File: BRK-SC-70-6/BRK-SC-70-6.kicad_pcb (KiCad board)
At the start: 2 copper layers, 18.3 x 18 mm, 3 parts, among them J1 Conn_01x03, J2 Conn_01x03, U1 SC-70-6

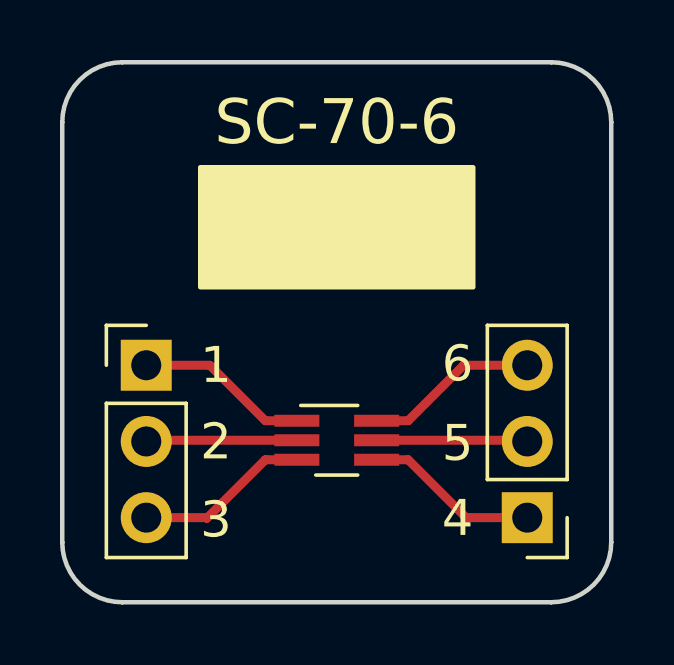
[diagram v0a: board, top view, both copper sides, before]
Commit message: Update several breakout boards
* Reduce distance from edge to pin header
* Enlarge silk screen area
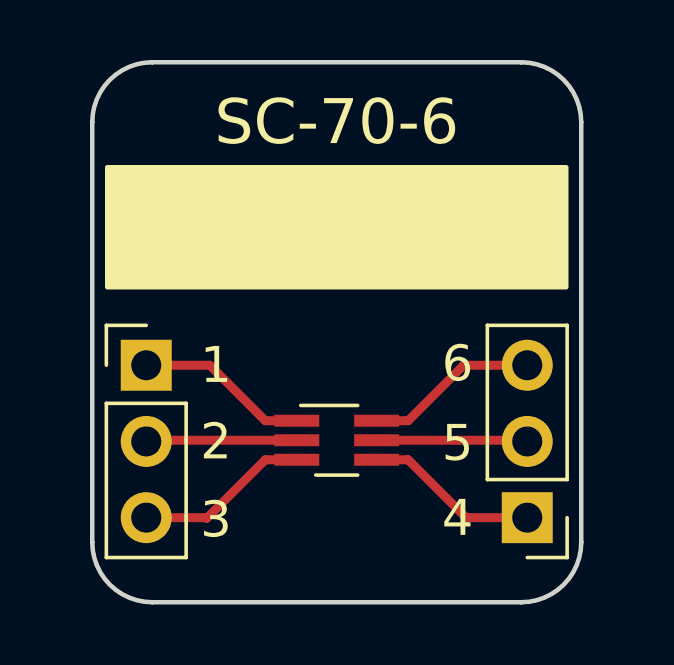
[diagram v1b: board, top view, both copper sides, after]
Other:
- board size 18.3 x 18 mm -> 16.3 x 18 mm
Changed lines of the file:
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@@
-(kicad_pcb (version 20171130) (host pcbnew 5.0.1-33cea8e~68~ubuntu18.10.1)
+(kicad_pcb (version 20171130) (host pcbnew 5.1.4-e60b266~84~ubuntu19.04.1)
   (general
-    (thickness 1.6)
+    (thickness 1)
     (drawings 16)
     (tracks 18)
@@
   (title_block
     (title BRK-SC-70-6)
-    (rev v1.0)
+    (rev v1.1)
     (company https://gekkio.fi)
   )
@@
     (zone_45_only no)
     (trace_min 0.2)
-    (segment_width 0.2)
-    (edge_width 0.15)
     (via_size 0.8)
     (via_drill 0.4)
@@
     (uvia_min_size 0.2)
     (uvia_min_drill 0.1)
+    (edge_width 0.15)
+    (segment_width 0.2)
     (pcb_text_width 0.3)
     (pcb_text_size 1.5 1.5)
@@
     (fp_line (start 1.27 -1.27) (end 1.27 6.35) (layer F.Fab) (width 0.1))
     (fp_line (start -0.635 -1.27) (end 1.27 -1.27) (layer F.Fab) (width 0.1))
-    (pad 3 thru_hole oval (at 0 5.08) (size 1.7 1.7) (drill 1) (layers *.Cu *.Mask)
+    (pad 3 thru_hole oval (at 0 5.08 180) (size 1.7 1.7) (drill 1) (layers *.Cu *.Mask)
       (net 6 "Net-(J2-Pad3)"))
-    (pad 2 thru_hole oval (at 0 2.54) (size 1.7 1.7) (drill 1) (layers *.Cu *.Mask)
+    (pad 2 thru_hole oval (at 0 2.54 180) (size 1.7 1.7) (drill 1) (layers *.Cu *.Mask)
       (net 5 "Net-(J2-Pad2)"))
-    (pad 1 thru_hole rect (at 0 0) (size 1.7 1.7) (drill 1) (layers *.Cu *.Mask)
+    (pad 1 thru_hole rect (at 0 0 180) (size 1.7 1.7) (drill 1) (layers *.Cu *.Mask)
       (net 4 "Net-(J2-Pad1)"))
     (model ${KISYS3DMOD}/Connector_PinHeader_2.54mm.3dshapes/PinHeader_1x03_P2.54mm_Vertical.wrl
@@
       (effects (font (size 1 1) (thickness 0.15)))
     )
+    (fp_text user %R (at 0 2.54 90) (layer F.Fab)
+      (effects (font (size 1 1) (thickness 0.15)))
+    )
+    (fp_line (start 1.8 -1.8) (end -1.8 -1.8) (layer F.CrtYd) (width 0.05))
+    (fp_line (start 1.8 6.85) (end 1.8 -1.8) (layer F.CrtYd) (width 0.05))
+    (fp_line (start -1.8 6.85) (end 1.8 6.85) (layer F.CrtYd) (width 0.05))
+    (fp_line (start -1.8 -1.8) (end -1.8 6.85) (layer F.CrtYd) (width 0.05))
+    (fp_line (start -1.33 -1.33) (end 0 -1.33) (layer F.SilkS) (width 0.12))
+    (fp_line (start -1.33 0) (end -1.33 -1.33) (layer F.SilkS) (width 0.12))
+    (fp_line (start -1.33 1.27) (end 1.33 1.27) (layer F.SilkS) (width 0.12))
+    (fp_line (start 1.33 1.27) (end 1.33 6.41) (layer F.SilkS) (width 0.12))
+    (fp_line (start -1.33 1.27) (end -1.33 6.41) (layer F.SilkS) (width 0.12))
+    (fp_line (start -1.33 6.41) (end 1.33 6.41) (layer F.SilkS) (width 0.12))
+    (fp_line (start -1.27 -0.635) (end -0.635 -1.27) (layer F.Fab) (width 0.1))
+    (fp_line (start -1.27 6.35) (end -1.27 -0.635) (layer F.Fab) (width 0.1))
+    (fp_line (start 1.27 6.35) (end -1.27 6.35) (layer F.Fab) (width 0.1))
+    (fp_line (start 1.27 -1.27) (end 1.27 6.35) (layer F.Fab) (width 0.1))
     (fp_line (start -0.635 -1.27) (end 1.27 -1.27) (layer F.Fab) (width 0.1))
-    (fp_line (start 1.27 -1.27) (end 1.27 6.35) (layer F.Fab) (width 0.1))
-    (fp_line (start 1.27 6.35) (end -1.27 6.35) (layer F.Fab) (width 0.1))
-    (fp_line (start -1.27 6.35) (end -1.27 -0.635) (layer F.Fab) (width 0.1))
-    (fp_line (start -1.27 -0.635) (end -0.635 -1.27) (layer F.Fab) (width 0.1))
-    (fp_line (start -1.33 6.41) (end 1.33 6.41) (layer F.SilkS) (width 0.12))
-    (fp_line (start -1.33 1.27) (end -1.33 6.41) (layer F.SilkS) (width 0.12))
-    (fp_line (start 1.33 1.27) (end 1.33 6.41) (layer F.SilkS) (width 0.12))
-    (fp_line (start -1.33 1.27) (end 1.33 1.27) (layer F.SilkS) (width 0.12))
-    (fp_line (start -1.33 0) (end -1.33 -1.33) (layer F.SilkS) (width 0.12))
-    (fp_line (start -1.33 -1.33) (end 0 -1.33) (layer F.SilkS) (width 0.12))
-    (fp_line (start -1.8 -1.8) (end -1.8 6.85) (layer F.CrtYd) (width 0.05))
-    (fp_line (start -1.8 6.85) (end 1.8 6.85) (layer F.CrtYd) (width 0.05))
-    (fp_line (start 1.8 6.85) (end 1.8 -1.8) (layer F.CrtYd) (width 0.05))
-    (fp_line (start 1.8 -1.8) (end -1.8 -1.8) (layer F.CrtYd) (width 0.05))
-    (fp_text user %R (at 0 2.54 90) (layer F.Fab)
-      (effects (font (size 1 1) (thickness 0.15)))
-    )
+    (pad 3 thru_hole oval (at 0 5.08) (size 1.7 1.7) (drill 1) (layers *.Cu *.Mask)
+      (net 3 "Net-(J1-Pad3)"))
+    (pad 2 thru_hole oval (at 0 2.54) (size 1.7 1.7) (drill 1) (layers *.Cu *.Mask)
+      (net 2 "Net-(J1-Pad2)"))
     (pad 1 thru_hole rect (at 0 0) (size 1.7 1.7) (drill 1) (layers *.Cu *.Mask)
       (net 1 "Net-(J1-Pad1)"))
-    (pad 2 thru_hole oval (at 0 2.54) (size 1.7 1.7) (drill 1) (layers *.Cu *.Mask)
-      (net 2 "Net-(J1-Pad2)"))
-    (pad 3 thru_hole oval (at 0 5.08) (size 1.7 1.7) (drill 1) (layers *.Cu *.Mask)
-      (net 3 "Net-(J1-Pad3)"))
     (model ${KISYS3DMOD}/Connector_PinHeader_2.54mm.3dshapes/PinHeader_1x03_P2.54mm_Vertical.wrl
       (at (xyz 0 0 0))
@@
       (effects (font (size 1 1) (thickness 0.15)))
     )
+    (fp_line (start -0.175 -1.1) (end -0.675 -0.6) (layer F.Fab) (width 0.1))
+    (fp_line (start 0.675 1.1) (end -0.675 1.1) (layer F.Fab) (width 0.1))
+    (fp_line (start 0.675 -1.1) (end 0.675 1.1) (layer F.Fab) (width 0.1))
+    (fp_line (start -0.675 -0.6) (end -0.675 1.1) (layer F.Fab) (width 0.1))
+    (fp_line (start 0.675 -1.1) (end -0.175 -1.1) (layer F.Fab) (width 0.1))
+    (fp_line (start -2.4 -1.4) (end 2.4 -1.4) (layer F.CrtYd) (width 0.05))
+    (fp_line (start -2.4 -1.4) (end -2.4 1.4) (layer F.CrtYd) (width 0.05))
+    (fp_line (start 2.4 1.4) (end 2.4 -1.4) (layer F.CrtYd) (width 0.05))
+    (fp_line (start -0.7 1.16) (end 0.7 1.16) (layer F.SilkS) (width 0.12))
+    (fp_line (start 0.7 -1.16) (end -1.2 -1.16) (layer F.SilkS) (width 0.12))
+    (fp_line (start -2.4 1.4) (end 2.4 1.4) (layer F.CrtYd) (width 0.05))
     (fp_text user %R (at 0 0 90) (layer F.Fab)
       (effects (font (size 0.5 0.5) (thickness 0.075)))
     )
-    (fp_line (start -2.4 1.4) (end 2.4 1.4) (layer F.CrtYd) (width 0.05))
-    (fp_line (start 0.7 -1.16) (end -1.2 -1.16) (layer F.SilkS) (width 0.12))
-    (fp_line (start -0.7 1.16) (end 0.7 1.16) (layer F.SilkS) (width 0.12))
-    (fp_line (start 2.4 1.4) (end 2.4 -1.4) (layer F.CrtYd) (width 0.05))
-    (fp_line (start -2.4 -1.4) (end -2.4 1.4) (layer F.CrtYd) (width 0.05))
-    (fp_line (start -2.4 -1.4) (end 2.4 -1.4) (layer F.CrtYd) (width 0.05))
-    (fp_line (start 0.675 -1.1) (end -0.175 -1.1) (layer F.Fab) (width 0.1))
-    (fp_line (start -0.675 -0.6) (end -0.675 1.1) (layer F.Fab) (width 0.1))
-    (fp_line (start 0.675 -1.1) (end 0.675 1.1) (layer F.Fab) (width 0.1))
-    (fp_line (start 0.675 1.1) (end -0.675 1.1) (layer F.Fab) (width 0.1))
-    (fp_line (start -0.175 -1.1) (end -0.675 -0.6) (layer F.Fab) (width 0.1))
+    (pad 6 smd rect (at 1.33 -0.65) (size 1.5 0.4) (layers F.Cu F.Paste F.Mask)
+      (net 6 "Net-(J2-Pad3)"))
+    (pad 5 smd rect (at 1.33 0) (size 1.5 0.4) (layers F.Cu F.Paste F.Mask)
+      (net 5 "Net-(J2-Pad2)"))
+    (pad 4 smd rect (at 1.33 0.65) (size 1.5 0.4) (layers F.Cu F.Paste F.Mask)
+      (net 4 "Net-(J2-Pad1)"))
+    (pad 3 smd rect (at -1.33 0.65) (size 1.5 0.4) (layers F.Cu F.Paste F.Mask)
+      (net 3 "Net-(J1-Pad3)"))
+    (pad 2 smd rect (at -1.33 0) (size 1.5 0.4) (layers F.Cu F.Paste F.Mask)
+      (net 2 "Net-(J1-Pad2)"))
     (pad 1 smd rect (at -1.33 -0.65) (size 1.5 0.4) (layers F.Cu F.Paste F.Mask)
       (net 1 "Net-(J1-Pad1)"))
-    (pad 2 smd rect (at -1.33 0) (size 1.5 0.4) (layers F.Cu F.Paste F.Mask)
-      (net 2 "Net-(J1-Pad2)"))
-    (pad 3 smd rect (at -1.33 0.65) (size 1.5 0.4) (layers F.Cu F.Paste F.Mask)
-      (net 3 "Net-(J1-Pad3)"))
-    (pad 4 smd rect (at 1.33 0.65) (size 1.5 0.4) (layers F.Cu F.Paste F.Mask)
-      (net 4 "Net-(J2-Pad1)"))
-    (pad 5 smd rect (at 1.33 0) (size 1.5 0.4) (layers F.Cu F.Paste F.Mask)
-      (net 5 "Net-(J2-Pad2)"))
-    (pad 6 smd rect (at 1.33 -0.65) (size 1.5 0.4) (layers F.Cu F.Paste F.Mask)
-      (net 6 "Net-(J2-Pad3)"))
     (model ${KISYS3DMOD}/Package_TO_SOT_SMD.3dshapes/SOT-363_SC-70-6.wrl
       (at (xyz 0 0 0))
@@
     )
   )
-  (gr_arc (start 52 66) (end 50 66) (angle -90) (layer Edge.Cuts) (width 0.15))
-  (gr_arc (start 66.3 66) (end 66.3 68) (angle -90) (layer Edge.Cuts) (width 0.15))
-  (gr_arc (start 66.3 52) (end 68.3 52) (angle -90) (layer Edge.Cuts) (width 0.15))
-  (gr_arc (start 52 52) (end 52 50) (angle -90) (layer Edge.Cuts) (width 0.15))
+  (gr_arc (start 53 66) (end 51 66) (angle -90) (layer Edge.Cuts) (width 0.15))
+  (gr_arc (start 65.3 66) (end 65.3 68) (angle -90) (layer Edge.Cuts) (width 0.15))
+  (gr_arc (start 65.3 52) (end 67.3 52) (angle -90) (layer Edge.Cuts) (width 0.15))
+  (gr_arc (start 53 52) (end 53 50) (angle -90) (layer Edge.Cuts) (width 0.15))
   (gr_text 4 (at 63.7 65.2) (layer F.SilkS)
     (effects (font (size 1.2 1.2) (thickness 0.3)) (justify right))
@@
     (effects (font (size 1.2 1.2) (thickness 0.3)) (justify left))
   )
-  (gr_line (start 66.3 68) (end 52 68) (layer Edge.Cuts) (width 0.15))
-  (gr_poly (pts (xy 54.6 53.5) (xy 54.6 57.5) (xy 63.7 57.5) (xy 63.7 53.5)) (layer F.SilkS) (width 0.15))
-  (gr_line (start 68.3 52) (end 68.3 66) (layer Edge.Cuts) (width 0.15))
+  (gr_line (start 65.3 68) (end 53 68) (layer Edge.Cuts) (width 0.15))
+  (gr_poly (pts (xy 51.5 53.5) (xy 51.5 57.5) (xy 66.8 57.5) (xy 66.8 53.5)) (layer F.SilkS) (width 0.15))
+  (gr_line (start 67.3 52) (end 67.3 66) (layer Edge.Cuts) (width 0.15))
   (gr_text SC-70-6 (at 59.15 52) (layer F.SilkS)
     (effects (font (size 1.5 1.5) (thickness 0.3)))
   )
-  (gr_line (start 52 50) (end 66.3 50) (layer Edge.Cuts) (width 0.15))
-  (gr_line (start 50 66) (end 50 52) (layer Edge.Cuts) (width 0.15))
+  (gr_line (start 53 50) (end 65.3 50) (layer Edge.Cuts) (width 0.15))
+  (gr_line (start 51 66) (end 51 52) (layer Edge.Cuts) (width 0.15))
   (segment (start 56.77 61.95) (end 54.92 60.1) (width 0.3) (layer F.Cu) (net 1))
   (segment (start 57.82 61.95) (end 56.77 61.95) (width 0.3) (layer F.Cu) (net 1))
